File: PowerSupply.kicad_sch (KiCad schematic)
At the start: 32 parts, among them IC3 MAX17048G+T10, IC4 BQ24074RGTR, SW3 SW_DPDT_x2, U4 1043, U5 1043, U6 LD1086DT33TR, U7 LD1086DT33TR

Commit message: routing
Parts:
- C14: value (none) -> 1u; footprint (none) -> Capacitor_SMD:C_0603_1608Metric_Pad1.08x0.95mm_HandSolder
- C15, C17: value (none) -> 4u7; footprint (none) -> Capacitor_SMD:C_0603_1608Metric_Pad1.08x0.95mm_HandSolder
- C16: value (none) -> 0.1u; footprint (none) -> Capacitor_SMD:C_0603_1608Metric_Pad1.08x0.95mm_HandSolder
- D4: value (none) -> LOW_BATTERY; footprint (none) -> LED_SMD:LED_0805_2012Metric_Pad1.15x1.40mm_HandSolder
- R10: value (none) -> 1k; footprint (none) -> Resistor_SMD:R_0603_1608Metric_Pad0.98x0.95mm_HandSolder
- R11: value (none) -> 820; footprint (none) -> Resistor_SMD:R_0603_1608Metric_Pad0.98x0.95mm_HandSolder
- R14: value (none) -> 1k5; footprint (none) -> Resistor_SMD:R_0805_2012Metric_Pad1.20x1.40mm_HandSolder
- R9: value (none) -> 10k; footprint (none) -> Resistor_SMD:R_0603_1608Metric_Pad0.98x0.95mm_HandSolder
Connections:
- net GND: no longer C20.2, C22.2, D6.1 (K), U7.1 (ADJ/GND)
- new net GNDA: C20.2, C22.2, D6.1 (K), U7.1 (ADJ/GND)
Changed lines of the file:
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@@
+    (pin "1")
+  )
+  (symbol (lib_id "power:GNDA") (at 243.84 99.06 0) (unit 1)
+    (in_bom yes) (on_board yes) (fields_autoplaced)
+    (property "Reference" "#PWR0155" (id 0) (at 243.84 105.41 0)
+      (effects (font (size 1.27 1.27)) hide)
+    )
+    (property "Value" "GNDA" (id 1) (at 243.84 104.14 0))
+    (property "Footprint" "" (id 2) (at 243.84 99.06 0)
+      (effects (font (size 1.27 1.27)) hide)
+    )
+    (property "Datasheet" "" (id 3) (at 243.84 99.06 0)
+      (effects (font (size 1.27 1.27)) hide)
+    )
     (pin "1")
   )
@@
       (effects (font (size 1.27 1.27)) (justify left))
     )
-    (property "Value" "" (id 1) (at 158.75 104.1462 0)
-      (effects (font (size 1.27 1.27)) (justify left))
-    )
-    (property "Footprint" "" (id 2) (at 156.21 102.87 0)
+    (property "Value" "4u7" (id 1) (at 158.75 104.1462 0)
+      (effects (font (size 1.27 1.27)) (justify left))
+    )
+    (property "Footprint" "Capacitor_SMD:C_0603_1608Metric_Pad1.08x0.95mm_HandSolder" (id 2) (at 156.21 102.87 0)
       (effects (font (size 1.27 1.27)) hide)
     )
@@
       (effects (font (size 1.27 1.27)) (justify left))
     )
-    (property "Value" "" (id 1) (at 134.62 134.62 0)
-      (effects (font (size 1.27 1.27)) (justify left))
-    )
-    (property "Footprint" "" (id 2) (at 132.08 133.35 0)
+    (property "Value" "820" (id 1) (at 134.62 134.62 0)
+      (effects (font (size 1.27 1.27)) (justify left))
+    )
+    (property "Footprint" "Resistor_SMD:R_0603_1608Metric_Pad0.98x0.95mm_HandSolder" (id 2) (at 132.08 133.35 0)
       (effects (font (size 1.27 1.27)) hide)
     )
@@
     (pin "1")
   )
+  (symbol (lib_id "power:GNDA") (at 201.93 96.52 0) (unit 1)
+    (in_bom yes) (on_board yes) (fields_autoplaced)
+    (property "Reference" "#PWR0156" (id 0) (at 201.93 102.87 0)
+      (effects (font (size 1.27 1.27)) hide)
+    )
+    (property "Value" "GNDA" (id 1) (at 201.93 101.6 0))
+    (property "Footprint" "" (id 2) (at 201.93 96.52 0)
+      (effects (font (size 1.27 1.27)) hide)
+    )
+    (property "Datasheet" "" (id 3) (at 201.93 96.52 0)
+      (effects (font (size 1.27 1.27)) hide)
+    )
+    (pin "1")
+  )
   (symbol (lib_id "power:GND") (at 151.13 119.38 0) (unit 1)
     (in_bom yes) (on_board yes) (fields_autoplaced)
@@
     )
     (property "Datasheet" "" (id 3) (at 232.41 62.23 0)
-      (effects (font (size 1.27 1.27)) hide)
-    )
-    (pin "1")
-  )
-  (symbol (lib_id "power:GND") (at 218.44 96.52 0) (unit 1)
-    (in_bom yes) (on_board yes) (fields_autoplaced)
-    (property "Reference" "#PWR043" (id 0) (at 218.44 102.87 0)
-      (effects (font (size 1.27 1.27)) hide)
-    )
-    (property "Value" "GND" (id 1) (at 218.44 101.6 0))
-    (property "Footprint" "" (id 2) (at 218.44 96.52 0)
-      (effects (font (size 1.27 1.27)) hide)
-    )
-    (property "Datasheet" "" (id 3) (at 218.44 96.52 0)
       (effects (font (size 1.27 1.27)) hide)
     )
@@
       (effects (font (size 1.27 1.27)) (justify left))
     )
-    (property "Value" "" (id 1) (at 105.41 119.3862 0)
-      (effects (font (size 1.27 1.27)) (justify left))
-    )
-    (property "Footprint" "" (id 2) (at 102.87 118.11 0)
+    (property "Value" "4u7" (id 1) (at 105.41 119.3862 0)
+      (effects (font (size 1.27 1.27)) (justify left))
+    )
+    (property "Footprint" "Capacitor_SMD:C_0603_1608Metric_Pad1.08x0.95mm_HandSolder" (id 2) (at 102.87 118.11 0)
       (effects (font (size 1.27 1.27)) hide)
     )
@@
       (effects (font (size 1.27 1.27)) (justify left))
     )
-    (property "Value" "" (id 1) (at 160.02 46.99 0)
-      (effects (font (size 1.27 1.27)) (justify left))
-    )
-    (property "Footprint" "" (id 2) (at 157.48 45.72 0)
+    (property "Value" "1k5" (id 1) (at 160.02 46.99 0)
+      (effects (font (size 1.27 1.27)) (justify left))
+    )
+    (property "Footprint" "Resistor_SMD:R_0805_2012Metric_Pad1.20x1.40mm_HandSolder" (id 2) (at 157.48 45.72 0)
       (effects (font (size 1.27 1.27)) hide)
     )
@@
     (pin "2")
   )
-  (symbol (lib_id "power:GND") (at 201.93 96.52 0) (unit 1)
-    (in_bom yes) (on_board yes) (fields_autoplaced)
-    (property "Reference" "#PWR041" (id 0) (at 201.93 102.87 0)
-      (effects (font (size 1.27 1.27)) hide)
-    )
-    (property "Value" "GND" (id 1) (at 201.93 101.6 0))
-    (property "Footprint" "" (id 2) (at 201.93 96.52 0)
-      (effects (font (size 1.27 1.27)) hide)
-    )
-    (property "Datasheet" "" (id 3) (at 201.93 96.52 0)
-      (effects (font (size 1.27 1.27)) hide)
-    )
-    (pin "1")
-  )
   (symbol (lib_id "Connector:TestPoint") (at 68.58 116.84 0) (unit 1)
     (in_bom yes) (on_board yes) (fields_autoplaced)
@@
       (effects (font (size 1.27 1.27)) (justify left))
     )
-    (property "Value" "" (id 1) (at 105.41 102.8762 0)
-      (effects (font (size 1.27 1.27)) (justify left))
-    )
-    (property "Footprint" "" (id 2) (at 102.87 101.6 0)
+    (property "Value" "1u" (id 1) (at 105.41 102.8762 0)
+      (effects (font (size 1.27 1.27)) (justify left))
+    )
+    (property "Footprint" "Capacitor_SMD:C_0603_1608Metric_Pad1.08x0.95mm_HandSolder" (id 2) (at 102.87 101.6 0)
       (effects (font (size 1.27 1.27)) hide)
     )
@@
       (effects (font (size 1.27 1.27)) (justify left))
     )
-    (property "Value" "" (id 1) (at 125.73 134.62 0)
-      (effects (font (size 1.27 1.27)) (justify left))
-    )
-    (property "Footprint" "" (id 2) (at 128.27 133.35 0)
+    (property "Value" "1k" (id 1) (at 125.73 134.62 0)
+      (effects (font (size 1.27 1.27)) (justify left))
+    )
+    (property "Footprint" "Resistor_SMD:R_0603_1608Metric_Pad0.98x0.95mm_HandSolder" (id 2) (at 128.27 133.35 0)
       (effects (font (size 1.27 1.27)) hide)
     )
@@
     (pin "2")
   )
+  (symbol (lib_id "power:GNDA") (at 232.41 96.52 0) (unit 1)
+    (in_bom yes) (on_board yes) (fields_autoplaced)
+    (property "Reference" "#PWR0158" (id 0) (at 232.41 102.87 0)
+      (effects (font (size 1.27 1.27)) hide)
+    )
+    (property "Value" "GNDA" (id 1) (at 232.41 101.6 0))
+    (property "Footprint" "" (id 2) (at 232.41 96.52 0)
+      (effects (font (size 1.27 1.27)) hide)
+    )
+    (property "Datasheet" "" (id 3) (at 232.41 96.52 0)
+      (effects (font (size 1.27 1.27)) hide)
+    )
+    (pin "1")
+  )
   (symbol (lib_id "Device:C_Small") (at 105.41 48.26 0) (unit 1)
     (in_bom yes) (on_board yes)
@@
       (effects (font (size 1.27 1.27)) (justify left))
     )
-    (property "Value" "" (id 1) (at 107.95 49.5362 0)
-      (effects (font (size 1.27 1.27)) (justify left))
-    )
-    (property "Footprint" "" (id 2) (at 105.41 48.26 0)
+    (property "Value" "0.1u" (id 1) (at 107.95 49.5362 0)
+      (effects (font (size 1.27 1.27)) (justify left))
+    )
+    (property "Footprint" "Capacitor_SMD:C_0603_1608Metric_Pad1.08x0.95mm_HandSolder" (id 2) (at 105.41 48.26 0)
       (effects (font (size 1.27 1.27)) hide)
     )
@@
       (effects (font (size 1.27 1.27)) (justify left))
     )
-    (property "Value" "" (id 1) (at 110.49 109.22 0)
-      (effects (font (size 1.27 1.27)) (justify left))
-    )
-    (property "Footprint" "" (id 2) (at 113.03 107.95 0)
+    (property "Value" "10k" (id 1) (at 110.49 109.22 0)
+      (effects (font (size 1.27 1.27)) (justify left))
+    )
+    (property "Footprint" "Resistor_SMD:R_0603_1608Metric_Pad0.98x0.95mm_HandSolder" (id 2) (at 113.03 107.95 0)
       (effects (font (size 1.27 1.27)) hide)
     )
@@
       (effects (font (size 1.27 1.27)) (justify left))
     )
-    (property "Value" "" (id 1) (at 160.02 52.0064 90)
-      (effects (font (size 1.27 1.27)) (justify left))
-    )
-    (property "Footprint" "" (id 2) (at 157.48 50.8 90)
+    (property "Value" "LOW_BATTERY" (id 1) (at 160.02 52.0064 90)
+      (effects (font (size 1.27 1.27)) (justify left))
+    )
+    (property "Footprint" "LED_SMD:LED_0805_2012Metric_Pad1.15x1.40mm_HandSolder" (id 2) (at 157.48 50.8 90)
       (effects (font (size 1.27 1.27)) hide)
     )
@@
     (pin "2")
   )
-  (symbol (lib_id "power:GND") (at 232.41 96.52 0) (unit 1)
-    (in_bom yes) (on_board yes) (fields_autoplaced)
-    (property "Reference" "#PWR048" (id 0) (at 232.41 102.87 0)
-      (effects (font (size 1.27 1.27)) hide)
-    )
-    (property "Value" "GND" (id 1) (at 232.41 101.6 0))
-    (property "Footprint" "" (id 2) (at 232.41 96.52 0)
-      (effects (font (size 1.27 1.27)) hide)
-    )
-    (property "Datasheet" "" (id 3) (at 232.41 96.52 0)
+  (symbol (lib_id "power:GNDA") (at 218.44 96.52 0) (unit 1)
+    (in_bom yes) (on_board yes) (fields_autoplaced)
+    (property "Reference" "#PWR0157" (id 0) (at 218.44 102.87 0)
+      (effects (font (size 1.27 1.27)) hide)
+    )
+    (property "Value" "GNDA" (id 1) (at 218.44 101.6 0))
+    (property "Footprint" "" (id 2) (at 218.44 96.52 0)
+      (effects (font (size 1.27 1.27)) hide)
+    )
+    (property "Datasheet" "" (id 3) (at 218.44 96.52 0)
       (effects (font (size 1.27 1.27)) hide)
     )
@@
     (pin "2")
   )
-  (symbol (lib_id "power:GND") (at 243.84 99.06 0) (unit 1)
-    (in_bom yes) (on_board yes) (fields_autoplaced)
-    (property "Reference" "#PWR051" (id 0) (at 243.84 105.41 0)
-      (effects (font (size 1.27 1.27)) hide)
-    )
-    (property "Value" "GND" (id 1) (at 243.84 104.14 0))
-    (property "Footprint" "" (id 2) (at 243.84 99.06 0)
-      (effects (font (size 1.27 1.27)) hide)
-    )
-    (property "Datasheet" "" (id 3) (at 243.84 99.06 0)
-      (effects (font (size 1.27 1.27)) hide)
-    )
-    (pin "1")
-  )
   (symbol (lib_id "project_library:1043") (at 54.61 104.14 0) (mirror y) (unit 1)

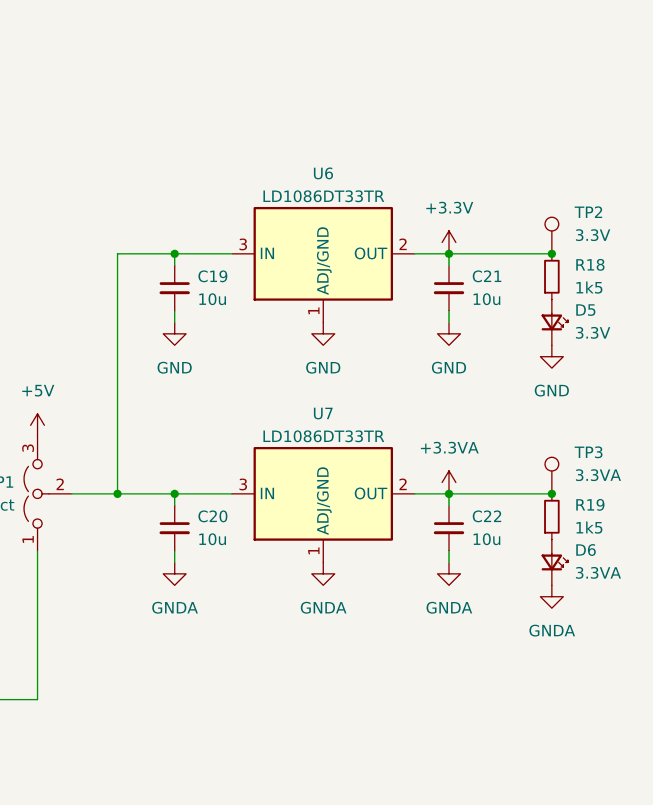
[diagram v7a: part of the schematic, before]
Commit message: changed linear regulators
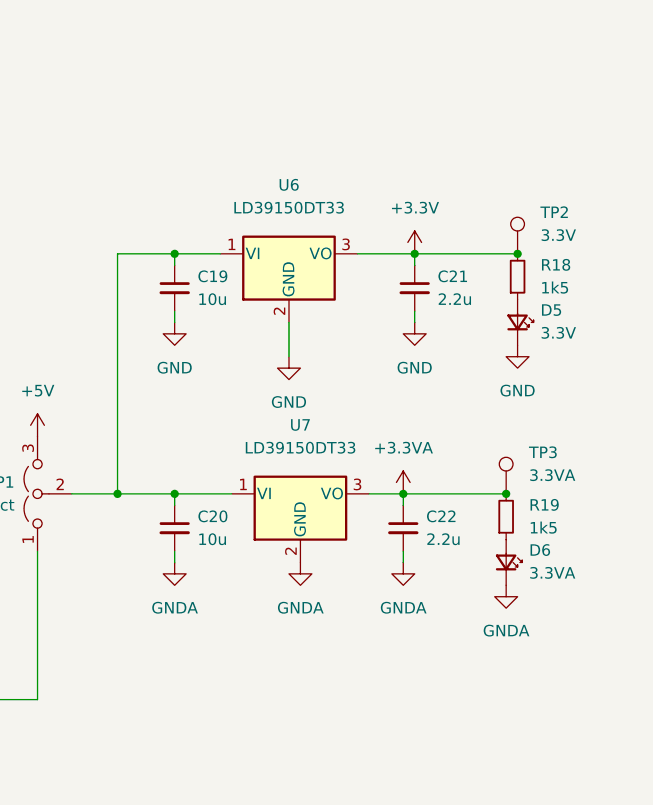
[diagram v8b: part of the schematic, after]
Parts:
- removed U6, U7: LD1086DT33TR, Package_TO_SOT_SMD:TO-252-2, symbol Regulator_Linear:LD1086DT33TR
- added U6, U7: LD39150DT33, Package_TO_SOT_SMD:TO-252-3_TabPin2, symbol Regulator_Linear:LD39150DT33
- C21, C22: value 10u -> 2.2u
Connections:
- net +3.3VA: now also U7.3 (VO)
- net +3V3: now also U6.3 (VO)
- net GND: now also U6.2 (GND)
- net GNDA: now also U7.2 (GND)
- net at C19.1, C20.1, JP1.2 (C): now also U6.1 (VI), U7.1 (VI)
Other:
- moved on the sheet: C21, C22, D5, D6, R18, R19, TP2, TP3
